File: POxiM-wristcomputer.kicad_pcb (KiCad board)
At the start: 4 copper layers, 40 x 23.5 mm, 62 parts, among them J1 USB_B_Micro, J2 AudioJack4_Ground, U1 LM321, U2 STM8S003F3P

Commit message: Finish display tester board Rev A
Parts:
- removed C1, C3, C5, C8, C9: 100nF, Capacitor_SMD:C_0603_1608Metric
- removed C2: 100pF, Capacitor_SMD:C_0603_1608Metric
- removed C4, C6: 2.2uF, Capacitor_SMD:C_0805_2012Metric
- removed C7: 470nF, Capacitor_SMD:C_0603_1608Metric
- removed D1, D3, D31, D5: 5.2V, Diode_SMD:D_SOD-123
- removed D2, D32, D4, D6: ~, Diode_SMD:D_SOD-323
- removed F1: 100mA, Resistor_SMD:R_1206_3216Metric
- removed FB1: Ferrite_Bead_Small, Inductor_SMD:L_0805_2012Metric
- removed JP1, JP2: Jumper_2_Open, Resistor_SMD:R_0603_1608Metric
- removed R1: 3.3MΩ, Resistor_SMD:R_0805_2012Metric
- removed R2: 1k, Resistor_SMD:R_0805_2012Metric
- removed R3, R4, R5: 100, Resistor_SMD:R_0805_2012Metric
- removed R6: R_Small, Resistor_SMD:R_0805_2012Metric
- removed U1: LM321, Package_TO_SOT_SMD:SOT-23-5
- removed U2: STM8S003F3P, Package_SO:TSSOP-20_4.4x6.5mm_P0.65mm
- added G***: LOGO, POxiM-logos:TUDelftLogo_W10mm, F.Cu at (86.4, 142.8)
- added G***: LOGO, POxiM-logos:POxiMLogo_GoldHeart_W7_5mm, F.Cu at (78.7, 123.0)
- added J14: Jumper_NO_Small, POxiM-uncategorised:SolderJumper-2_P1.3mm_Open_RoundedPad1.0x1.5mm, B.Cu at (99.7, 143.6)
- added JP10: Jumper_NC_Small, POxiM-uncategorised:SolderJumper-2_P1.3mm_SolderBridged_RoundedPad1.0x1.5mm, B.Cu at (101.5, 124.0)
- added JP11: Jumper_NC_Small, POxiM-uncategorised:SolderJumper-2_P1.3mm_SolderBridged_RoundedPad1.0x1.5mm, B.Cu at (80.5, 130.2)
- added JP12: Jumper_NC_Small, POxiM-uncategorised:SolderJumper-2_P1.3mm_SolderBridged_RoundedPad1.0x1.5mm, B.Cu at (101.2, 140.8)
- added JP13: Jumper_NC_Small, POxiM-uncategorised:SolderJumper-2_P1.3mm_SolderBridged_RoundedPad1.0x1.5mm, B.Cu at (80.2, 138.5)
- added JP15: Jumper_NC_Small, POxiM-uncategorised:SolderJumper-2_P1.3mm_SolderBridged_RoundedPad1.0x1.5mm, B.Cu at (78.2, 138.5)
- added JP16: Jumper_NO_Small, POxiM-uncategorised:SolderJumper-2_P1.3mm_Open_RoundedPad1.0x1.5mm, B.Cu at (99.2, 140.8)
- added JP17: Jumper_NC_Small, POxiM-uncategorised:SolderJumper-2_P1.3mm_SolderBridged_RoundedPad1.0x1.5mm, B.Cu at (76.2, 138.5)
- added JP18: Jumper_NO_Small, POxiM-uncategorised:SolderJumper-2_P1.3mm_Open_RoundedPad1.0x1.5mm, B.Cu at (95.5, 124.0)
- added JP19: Jumper_NC_Small, POxiM-uncategorised:SolderJumper-2_P1.3mm_SolderBridged_RoundedPad1.0x1.5mm, B.Cu at (78.5, 130.2)
- added JP20: Jumper_NO_Small, POxiM-uncategorised:SolderJumper-2_P1.3mm_Open_RoundedPad1.0x1.5mm, B.Cu at (97.5, 124.0)
- added JP21: Jumper_NC_Small, POxiM-uncategorised:SolderJumper-2_P1.3mm_SolderBridged_RoundedPad1.0x1.5mm, B.Cu at (78.2, 135.5)
- added JP22: Jumper_NC_Small, POxiM-uncategorised:SolderJumper-2_P1.3mm_SolderBridged_RoundedPad1.0x1.5mm, B.Cu at (90.0, 123.0)
- added JP23: Jumper_NC_Small, POxiM-uncategorised:SolderJumper-2_P1.3mm_SolderBridged_RoundedPad1.0x1.5mm, B.Cu at (75.8, 127.0)
- added JP24: Jumper_NC_Small, POxiM-uncategorised:SolderJumper-2_P1.3mm_SolderBridged_RoundedPad1.0x1.5mm, B.Cu at (93.5, 124.0)
- added JP25: Jumper_NC_Small, POxiM-uncategorised:SolderJumper-2_P1.3mm_SolderBridged_RoundedPad1.0x1.5mm, B.Cu at (103.5, 124.0)
- added JP26: Jumper_NC_Small, POxiM-uncategorised:SolderJumper-2_P1.3mm_SolderBridged_RoundedPad1.0x1.5mm, B.Cu at (89.8, 137.2)
- added JP27: Jumper_NO_Small, POxiM-uncategorised:SolderJumper-2_P1.3mm_Open_RoundedPad1.0x1.5mm, B.Cu at (103.2, 140.8)
- added JP28: Jumper_NO_Small, POxiM-uncategorised:SolderJumper-2_P1.3mm_Open_RoundedPad1.0x1.5mm, B.Cu at (90.0, 143.5)
- added JP29: Jumper_NO_Small, POxiM-uncategorised:SolderJumper-2_P1.3mm_Open_RoundedPad1.0x1.5mm, B.Cu at (87.2, 137.2)
- added JP30: Jumper_NO_Small, POxiM-uncategorised:SolderJumper-2_P1.3mm_Open_RoundedPad1.0x1.5mm, B.Cu at (88.8, 129.2)
- added JP31: Jumper_NO_Small, POxiM-uncategorised:SolderJumper-2_P1.3mm_Open_RoundedPad1.0x1.5mm, B.Cu at (91.0, 129.2)
- added JP8: Jumper_NO_Small, POxiM-uncategorised:SolderJumper-2_P1.3mm_Open_RoundedPad1.0x1.5mm, B.Cu at (99.5, 124.0)
- added JP9: Jumper_NC_Small, POxiM-uncategorised:SolderJumper-2_P1.3mm_SolderBridged_RoundedPad1.0x1.5mm, B.Cu at (78.2, 123.0)
- added R10: 4.7kΩ, Resistor_SMD:R_0805_2012Metric_Pad1.15x1.40mm_HandSolder, B.Cu at (82.5, 130.2)
- added R11: 4.7kΩ, Resistor_SMD:R_0805_2012Metric_Pad1.15x1.40mm_HandSolder, B.Cu at (101.2, 137.2)
- added R12: 4.7kΩ, Resistor_SMD:R_0805_2012Metric_Pad1.15x1.40mm_HandSolder, B.Cu at (82.2, 138.5)
- added R13: 4.7kΩ, Resistor_SMD:R_0805_2012Metric_Pad1.15x1.40mm_HandSolder, B.Cu at (103.2, 143.5)
- added R14: 4.7kΩ, Resistor_SMD:R_0805_2012Metric_Pad1.15x1.40mm_HandSolder, B.Cu at (78.2, 141.2)
- added R15: 4.7kΩ, Resistor_SMD:R_0805_2012Metric_Pad1.15x1.40mm_HandSolder, B.Cu at (99.2, 137.2)
- added R16: 4.7kΩ, Resistor_SMD:R_0805_2012Metric_Pad1.15x1.40mm_HandSolder, B.Cu at (74.0, 138.5)
- added R17: 4.7kΩ, Resistor_SMD:R_0805_2012Metric_Pad1.15x1.40mm_HandSolder, B.Cu at (95.5, 127.8)
- added R18: 4.7kΩ, Resistor_SMD:R_0805_2012Metric_Pad1.15x1.40mm_HandSolder, B.Cu at (76.2, 130.2)
- added R19: 4.7kΩ, Resistor_SMD:R_0805_2012Metric_Pad1.15x1.40mm_HandSolder, B.Cu at (97.5, 127.8)
- added R20: 4.7kΩ, Resistor_SMD:R_0805_2012Metric_Pad1.15x1.40mm_HandSolder, B.Cu at (78.2, 133.2)
- added R21: 4.7kΩ, Resistor_SMD:R_0805_2012Metric_Pad1.15x1.40mm_HandSolder, B.Cu at (90.0, 125.2)
- added R22: 4.7kΩ, Resistor_SMD:R_0805_2012Metric_Pad1.15x1.40mm_HandSolder, B.Cu at (72.2, 127.0)
- added R23: 4.7kΩ, Resistor_SMD:R_0805_2012Metric_Pad1.15x1.40mm_HandSolder, B.Cu at (93.5, 127.8)
- added R24: 4.7kΩ, Resistor_SMD:R_0805_2012Metric_Pad1.15x1.40mm_HandSolder, B.Cu at (104.8, 126.8)
- added R25: 4.7kΩ, Resistor_SMD:R_0805_2012Metric_Pad1.15x1.40mm_HandSolder, B.Cu at (92.0, 137.2)
- added R26: 4.7kΩ, Resistor_SMD:R_0805_2012Metric_Pad1.15x1.40mm_HandSolder, B.Cu at (103.2, 137.2)
- added R27: 4.7kΩ, Resistor_SMD:R_0805_2012Metric_Pad1.15x1.40mm_HandSolder, B.Cu at (90.0, 141.2)
- added R28: 4.7kΩ, Resistor_SMD:R_0805_2012Metric_Pad1.15x1.40mm_HandSolder, B.Cu at (85.0, 137.2)
- added R29: 4.7kΩ, Resistor_SMD:R_0805_2012Metric_Pad1.15x1.40mm_HandSolder, B.Cu at (86.5, 129.2)
- added R30: 4.7kΩ, Resistor_SMD:R_0805_2012Metric_Pad1.15x1.40mm_HandSolder, B.Cu at (90.0, 133.2)
- added R8: 4.7kΩ, Resistor_SMD:R_0805_2012Metric_Pad1.15x1.40mm_HandSolder, B.Cu at (78.2, 125.0)
- added R9: 4.7kΩ, Resistor_SMD:R_0805_2012Metric_Pad1.15x1.40mm_HandSolder, B.Cu at (101.5, 127.8)
- R7: value R_Small -> 4.7kΩ; footprint Resistor_SMD:R_0805_2012Metric -> Resistor_SMD:R_0805_2012Metric_Pad1.15x1.40mm_HandSolder
- moved R7 12.2 mm to (99.5, 127.8), turned to 270 degrees
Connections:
- D10 pad 1: /Display/Segment1 -> GND
- D11 pad 1: /Display/Segment2 -> GND
- D12 pad 1: /Display/Segment2 -> GND
- D12 pad 2: Net-(D10-Pad2) -> Net-(D12-Pad2)
- D13 pad 1: /Display/Segment3 -> GND
- D13 pad 2: Net-(D11-Pad2) -> Net-(D13-Pad2)
- D14 pad 1: /Display/Segment3 -> GND
- D14 pad 2: Net-(D10-Pad2) -> Net-(D14-Pad2)
- D15 pad 1: /Display/Segment4 -> GND
- D15 pad 2: Net-(D11-Pad2) -> Net-(D15-Pad2)
- D16 pad 1: /Display/Segment4 -> GND
- D16 pad 2: Net-(D10-Pad2) -> Net-(D16-Pad2)
- D17 pad 1: /Display/Segment5 -> GND
- D17 pad 2: Net-(D11-Pad2) -> Net-(D17-Pad2)
- D18 pad 1: /Display/Segment5 -> GND
- D18 pad 2: Net-(D10-Pad2) -> Net-(D18-Pad2)
- D19 pad 1: /Display/Segment6 -> GND
- D19 pad 2: Net-(D11-Pad2) -> Net-(D19-Pad2)
- D20 pad 1: /Display/Segment6 -> GND
- D20 pad 2: Net-(D10-Pad2) -> Net-(D20-Pad2)
- D21 pad 1: Net-(D11-Pad2) -> GND
- D21 pad 2: /Display/Segment0 -> Net-(D21-Pad2)
- D22 pad 1: Net-(D10-Pad2) -> GND
- D22 pad 2: /Display/Segment0 -> Net-(D22-Pad2)
- D23 pad 1: Net-(D11-Pad2) -> GND
- D23 pad 2: /Display/Segment1 -> Net-(D23-Pad2)
- D24 pad 1: Net-(D10-Pad2) -> GND
- D24 pad 2: /Display/Segment1 -> Net-(D24-Pad2)
- D25 pad 1: Net-(D11-Pad2) -> GND
- D25 pad 2: /Display/Segment2 -> Net-(D25-Pad2)
- D26 pad 1: Net-(D10-Pad2) -> GND
- D26 pad 2: /Display/Segment2 -> Net-(D26-Pad2)
- D27 pad 1: Net-(D11-Pad2) -> GND
- D27 pad 2: /Display/Segment3 -> Net-(D27-Pad2)
- D28 pad 1: Net-(D11-Pad2) -> GND
- D28 pad 2: /Display/Segment4 -> Net-(D28-Pad2)
- D29 pad 1: Net-(D11-Pad2) -> GND
- D29 pad 2: /Display/Segment5 -> Net-(D29-Pad2)
- D30 pad 1: Net-(D11-Pad2) -> GND
- D30 pad 2: /Display/Segment6 -> Net-(D30-Pad2)
- D7 pad 1: /Display/Segment0 -> GND
- D7 pad 2: Net-(D11-Pad2) -> Net-(D7-Pad2)
- D8 pad 1: /Display/Segment0 -> GND
- D8 pad 2: Net-(D10-Pad2) -> Net-(D8-Pad2)
- D9 pad 1: /Display/Segment1 -> GND
- D9 pad 2: Net-(D11-Pad2) -> Net-(D9-Pad2)
- J1 pad 1: /5V_power_input -> +5V
- J1 pad 2: /USB interface/Data- -> Net-(J1-Pad2)
- J1 pad 3: /USB interface/Data+ -> Net-(J1-Pad3)
- J2 pad R1: /Signal conditioning/LEDOut.IR -> Net-(J2-PadR1)
- J2 pad S: /Signal conditioning/PhotoDiode -> Net-(J2-PadS)
- J2 pad T: /Signal conditioning/LEDOut.Red -> Net-(J2-PadT)
- R7 pad 1: /Display/Common1 -> Net-(JP8-Pad2)
- R7 pad 2: Net-(D10-Pad2) -> Net-(D7-Pad2)
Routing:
- net +5V: track 0.00 -> 108.7 mm
- net GND: track 0.00 -> 10.4 mm, vias 0 -> 5
- net Net-(D9-Pad2): track 0.00 -> 8.21 mm, vias 0 -> 1
- net Net-(D23-Pad2): track 0.00 -> 8.07 mm, vias 0 -> 1
- net Net-(D11-Pad2): track 0.00 -> 7.72 mm, vias 0 -> 1
- net Net-(D17-Pad2): track 0.00 -> 7.47 mm, vias 0 -> 1
- net Net-(D7-Pad2): track 0.00 -> 7.12 mm, vias 0 -> 1
- net Net-(D19-Pad2): track 0.00 -> 6.59 mm, vias 0 -> 1
- net Net-(D18-Pad2): track 0.00 -> 6.50 mm, vias 0 -> 1
- net Net-(D26-Pad2): track 0.00 -> 6.11 mm, vias 0 -> 1
- net Net-(D13-Pad2): track 0.00 -> 5.32 mm, vias 0 -> 1
- net Net-(D16-Pad2): track 0.00 -> 5.09 mm, vias 0 -> 1
- net Net-(D25-Pad2): track 0.00 -> 5.07 mm, vias 0 -> 1
- net Net-(D24-Pad2): track 0.00 -> 5.07 mm, vias 0 -> 1
- net Net-(JP30-Pad2): track 0.00 -> 4.78 mm
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- added copper zone on B.Cu, net GND
- added copper zone on F.Cu, net GND
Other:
- net class Default: clearance 0.2 -> 0.1; trace_width 0.25 -> 0.1; via_dia 0.8 -> 0.4; via_drill 0.4 -> 0.2
- rule trace_clearance: 0.2 -> 0.1
- rule trace_min: 0.2 -> 0.1
- rule via_min_drill: 0.3 -> 0.2
- board text added: "Display test board Rev A"

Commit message: Finish works-as prototype design
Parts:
- removed the G*** at (86.4, 142.8)
- removed the G*** at (78.7, 123.0)
- removed J14, JP16, JP18, JP20, JP27, JP28, JP29, JP30, JP31, JP8: Jumper_NO_Small, POxiM-uncategorised:SolderJumper-2_P1.3mm_Open_RoundedPad1.0x1.5mm
- removed JP10, JP11, JP12, JP13, JP15, JP17, JP19, JP21, JP22, JP23, JP24, JP25, JP26, JP9: Jumper_NC_Small, POxiM-uncategorised:SolderJumper-2_P1.3mm_SolderBridged_RoundedPad1.0x1.5mm
- removed R20, R21, R22, R23, R24, R25, R26, R27, R28, R29, R30: 4.7kΩ, Resistor_SMD:R_0805_2012Metric_Pad1.15x1.40mm_HandSolder
- added C1: 100nF, Capacitor_SMD:C_0603_1608Metric, F.Cu at (182.7, 114.8)
- added C10: 2.2uF, Capacitor_SMD:C_0805_2012Metric, B.Cu at (128.0, 65.2)
- added C11: 100nF, Capacitor_SMD:C_0603_1608Metric, B.Cu at (128.0, 63.5)
- added C12: 100nF, Capacitor_SMD:C_0603_1608Metric, B.Cu at (123.2, 48.2)
- added C13: 2.2uF, Capacitor_SMD:C_0805_2012Metric, B.Cu at (121.5, 48.2)
- added C14: 6.8uF, Capacitor_SMD:C_1206_3216Metric, B.Cu at (115.5, 60.5)
- added C15: 6.8uF, Capacitor_SMD:C_1206_3216Metric, B.Cu at (140.5, 60.5)
- added C16: 100nF, Capacitor_SMD:C_0603_1608Metric, B.Cu at (109.2, 60.5)
- added C17: 100nF, Capacitor_SMD:C_0603_1608Metric, B.Cu at (146.8, 60.5)
- added C2: 100pF, Capacitor_SMD:C_0603_1608Metric, F.Cu at (188.2, 114.8)
- added C3: 100nF, Capacitor_SMD:C_0603_1608Metric, F.Cu at (188.2, 119.0)
- added C4: 2.2uF, Capacitor_SMD:C_0805_2012Metric, F.Cu at (182.0, 119.8)
- added C5: 100nF, Capacitor_SMD:C_0603_1608Metric, F.Cu at (171.2, 105.2)
- added C6: 2.2uF, Capacitor_SMD:C_0805_2012Metric, F.Cu at (164.0, 105.2)
- added C7: 470nF, Capacitor_SMD:C_0603_1608Metric, F.Cu at (168.8, 105.2)
- added C8: 100nF, Capacitor_SMD:C_0603_1608Metric, F.Cu at (165.8, 105.2)
- added C9: 100nF, Capacitor_SMD:C_0603_1608Metric, F.Cu at (167.2, 105.2)
- added D1: 5.2V, Diode_SMD:D_SOD-123, F.Cu at (176.5, 138.2)
- added D2: ~, Diode_SMD:D_SOD-323, F.Cu at (175.8, 136.0)
- added D3: 5.2V, Diode_SMD:D_SOD-123, F.Cu at (176.5, 127.0)
- added D31: 5.2V, Diode_SMD:D_SOD-123, F.Cu at (156.2, 134.5)
- added D32: ~, Diode_SMD:D_SOD-323, F.Cu at (155.8, 132.2)
- added D4: ~, Diode_SMD:D_SOD-323, F.Cu at (175.8, 129.2)
- added D5: 5.2V, Diode_SMD:D_SOD-123, F.Cu at (181.2, 122.0)
- added D6: ~, Diode_SMD:D_SOD-323, F.Cu at (177.2, 124.5)
- added F1: 100mA, Resistor_SMD:R_1206_3216Metric, F.Cu at (156.2, 137.0)
- added FB1: Ferrite_Bead_Small, Inductor_SMD:L_0603_1608Metric, F.Cu at (161.5, 106.0)
- added G***: LOGO, POxiM-logos:POxiMLogo_GoldHeart_W10mm, F.Cu at (120.0, 129.8)
- added G***: LOGO, POxiM-logos:TUDelftLogo_W10mm, F.Cu at (119.2, 132.8)
- added G***: LOGO, POxiM-logos:TUDelftLogo_W10mm, F.Cu at (157.8, 125.8)
- added G***: LOGO, POxiM-logos:POxiMLogo_GoldHeart_W10mm, F.Cu at (154.8, 125.0)
- added G***: LOGO, POxiM-logos:TUDelftLogo_W10mm, F.Cu at (184.2, 44.2)
- added G***: LOGO, POxiM-logos:POxiMLogo_GoldHeart_W20mm, F.Cu at (119.2, 44.0)
- added J10: Transmissivity in, Connector_Coaxial:SMA_Molex_73251-2200_Horizontal, F.Cu at (95.0, 60.5)
- added J11: AudioJack4_Ground, POxiM-uncategorised:CUI_SJ-43514-SMT, F.Cu at (98.5, 45.5)
- added J3: USB_B_Micro, POxiM-uncategorised:Micro-B_Molex_105017-0001, F.Cu at (115.0, 140.0)
- added J4: USB_A, POxiM-uncategorised:USBA_87583-2010RLF, F.Cu at (104.0, 131.0)
- added J5: USB_A, POxiM-uncategorised:USBA_87583-2010RLF, F.Cu at (104.0, 109.0)
- added J6: Uart Out, Connector_PinHeader_2.54mm:PinHeader_1x02_P2.54mm_Vertical, F.Cu at (108.0, 118.7)
- added J7: Programming Header, Connector_PinHeader_2.54mm:PinHeader_2x05_P2.54mm_Vertical, F.Cu at (123.2, 118.7)
- added J8: USB_B_Micro, POxiM-uncategorised:Micro-B_Molex_105017-0001, F.Cu at (90.0, 91.0)
- added J9: Interference in, Connector_Coaxial:SMA_Molex_73251-2200_Horizontal, F.Cu at (95.0, 76.0)
- added JP1: Jumper_2_Open, Resistor_SMD:R_0603_1608Metric, F.Cu at (164.8, 132.8)
- added JP2: Jumper_2_Open, Resistor_SMD:R_0603_1608Metric, F.Cu at (163.0, 132.8)
- added MB1: Bumpon, POxiM-uncategorised:Bumpon-SJ-5007BK, B.Cu at (96.0, 131.0)
- added MB10: Bumpon, POxiM-uncategorised:Bumpon-SJ-5007BK, B.Cu at (184.0, 46.0)
- added MB11: Bumpon, POxiM-uncategorised:Bumpon-SJ-5007BK, B.Cu at (184.0, 91.5)
- added MB12: Bumpon, POxiM-uncategorised:Bumpon-SJ-5007BK, B.Cu at (96.0, 91.5)
- added MB2: Bumpon, POxiM-uncategorised:Bumpon-SJ-5007BK, B.Cu at (96.0, 109.0)
- added MB3: Bumpon, POxiM-uncategorised:Bumpon-SJ-5007BK, B.Cu at (121.0, 106.0)
- added MB4: Bumpon, POxiM-uncategorised:Bumpon-SJ-5007BK, B.Cu at (121.0, 134.0)
- added MB5: Bumpon, POxiM-uncategorised:Bumpon-SJ-5007BK, B.Cu at (139.5, 134.2)
- added MB6: Bumpon, POxiM-uncategorised:Bumpon-SJ-5007BK, B.Cu at (139.5, 105.8)
- added MB7: Bumpon, POxiM-uncategorised:Bumpon-SJ-5007BK, B.Cu at (184.0, 134.0)
- added MB8: Bumpon, POxiM-uncategorised:Bumpon-SJ-5007BK, B.Cu at (184.0, 106.0)
- added MB9: Bumpon, POxiM-uncategorised:Bumpon-SJ-5007BK, B.Cu at (96.0, 46.0)
- added R1: 3.3MΩ, Resistor_SMD:R_0805_2012Metric, F.Cu at (185.5, 117.8)
- added R2: 1k, Resistor_SMD:R_0805_2012Metric, F.Cu at (185.5, 119.8)
- added R3: 100, Resistor_SMD:R_0805_2012Metric, F.Cu at (185.5, 122.0)
- added R4: 100, Resistor_SMD:R_0805_2012Metric, F.Cu at (175.8, 131.2)
- added R5: 100, Resistor_SMD:R_0805_2012Metric, F.Cu at (175.8, 134.0)
- added R6: R_Small, Resistor_SMD:R_0805_2012Metric, F.Cu at (162.0, 111.5)
- added RV1: 1k, POxiM-uncategorised:Potentiometer_Bourns_PTV09A-1_Single_Vertical, F.Cu at (170.5, 64.0)
- added RV2: 1k, POxiM-uncategorised:Potentiometer_Bourns_PTV09A-1_Single_Vertical, F.Cu at (118.0, 64.0)
- added RV3: 1k, POxiM-uncategorised:Potentiometer_Bourns_PTV09A-1_Single_Vertical, F.Cu at (118.0, 91.0)
- added RV4: 1k, POxiM-uncategorised:Potentiometer_Bourns_PTV09A-1_Single_Vertical, F.Cu at (143.0, 64.0)
- added RV5: 1k, POxiM-uncategorised:Potentiometer_Bourns_PTV09A-1_Single_Vertical, F.Cu at (143.0, 91.0)
- added SW1: Current range, POxiM-uncategorised:SW_ESwitch_KC14A10.001NPS, F.Cu at (168.0, 81.5)
- added TP1: LED_IR, TestPoint:TestPoint_Loop_D2.60mm_Drill1.4mm_Beaded, F.Cu at (166.0, 119.0)
- added TP10: IR, TestPoint:TestPoint_Loop_D2.60mm_Drill1.4mm_Beaded, F.Cu at (147.5, 46.2)
- added TP11: R, TestPoint:TestPoint_Loop_D2.60mm_Drill1.4mm_Beaded, F.Cu at (171.5, 46.2)
- added TP12: IR, TestPoint:TestPoint_Loop_D2.60mm_Drill1.4mm_Beaded, F.Cu at (175.5, 46.2)
- added TP13: I_in, TestPoint:TestPoint_Loop_D2.60mm_Drill1.4mm_Beaded, F.Cu at (159.5, 46.2)
- added TP16: N, TestPoint:TestPoint_Loop_D2.60mm_Drill1.4mm_Beaded, F.Cu at (167.5, 46.2)
- added TP17: R, TestPoint:TestPoint_Loop_D2.60mm_Drill1.4mm_Beaded, F.Cu at (139.5, 46.2)
- added TP19: GND, TestPoint:TestPoint_Loop_D2.60mm_Drill1.4mm_Beaded, F.Cu at (162.0, 119.0)
- added TP2: LED_R, TestPoint:TestPoint_Loop_D2.60mm_Drill1.4mm_Beaded, F.Cu at (170.0, 119.0)
- added TP20: GND, TestPoint:TestPoint_Loop_D2.60mm_Drill1.4mm_Beaded, F.Cu at (182.5, 110.5)
- added TP3: ADC_FB, TestPoint:TestPoint_Loop_D2.60mm_Drill1.4mm_Beaded, F.Cu at (178.5, 117.8)
- added TP4: ADC_in, TestPoint:TestPoint_Loop_D2.60mm_Drill1.4mm_Beaded, F.Cu at (186.5, 110.5)
- added TP5: PD3, TestPoint:TestPoint_Loop_D2.60mm_Drill1.4mm_Beaded, F.Cu at (176.8, 109.8)
- added TP6: PD4, TestPoint:TestPoint_Loop_D2.60mm_Drill1.4mm_Beaded, F.Cu at (176.8, 105.8)
- added TP7: PD2, TestPoint:TestPoint_Loop_D2.60mm_Drill1.4mm_Beaded, F.Cu at (176.8, 113.8)
- added TP8: GND, TestPoint:TestPoint_Loop_D2.60mm_Drill1.4mm_Beaded, F.Cu at (143.5, 46.2)
- added TP9: GND, TestPoint:TestPoint_Loop_D2.60mm_Drill1.4mm_Beaded, F.Cu at (163.5, 46.2)
- added U1: LM321, Package_TO_SOT_SMD:SOT-23-5, F.Cu at (185.5, 114.8)
- added U2: STM8S003F3P, Package_SO:TSSOP-20_4.4x6.5mm_P0.65mm, F.Cu at (170.2, 110.8)
- added U3: LM358, Package_SO:SOIC-8_3.9x4.9mm_P1.27mm, B.Cu at (128.0, 60.0)
- added U4: NLAS4053, Package_SO:SOIC-16_3.9x9.9mm_P1.27mm, B.Cu at (128.0, 51.8)
- added mouse-bite-2.54mm-slot: VAL**, Panelization:mouse-bite-2.5mm-slot, F.Cu at (96.5, 98.8)
- added mouse-bite-2.54mm-slot: VAL**, Panelization:mouse-bite-2.5mm-slot, F.Cu at (128.2, 133.5)
- added mouse-bite-2.54mm-slot: VAL**, Panelization:mouse-bite-2.5mm-slot, F.Cu at (128.2, 106.5)
- added mouse-bite-2.54mm-slot: VAL**, Panelization:mouse-bite-2.5mm-slot, F.Cu at (120.5, 98.8)
- added mouse-bite-2.54mm-slot: VAL**, Panelization:mouse-bite-2.5mm-slot, F.Cu at (136.0, 98.8)
- added mouse-bite-2.54mm-slot: VAL**, Panelization:mouse-bite-2.5mm-slot, F.Cu at (183.5, 98.8)
- J1, J2: moved to F.Cu
- R10, R18, R19, R8, R9: value 4.7kΩ -> 27kΩ; footprint Resistor_SMD:R_0805_2012Metric_Pad1.15x1.40mm_HandSolder -> Resistor_SMD:R_0603_1608Metric
- R11: value 4.7kΩ -> 1kΩ; footprint Resistor_SMD:R_0805_2012Metric_Pad1.15x1.40mm_HandSolder -> Resistor_SMD:R_0603_1608Metric
- R12: value 4.7kΩ -> 4.7MΩ; footprint Resistor_SMD:R_0805_2012Metric_Pad1.15x1.40mm_HandSolder -> Resistor_SMD:R_0603_1608Metric
- R13: value 4.7kΩ -> 470kΩ; footprint Resistor_SMD:R_0805_2012Metric_Pad1.15x1.40mm_HandSolder -> Resistor_SMD:R_0603_1608Metric
- R14: value 4.7kΩ -> 47kΩ; footprint Resistor_SMD:R_0805_2012Metric_Pad1.15x1.40mm_HandSolder -> Resistor_SMD:R_0603_1608Metric
- R15: footprint Resistor_SMD:R_0805_2012Metric_Pad1.15x1.40mm_HandSolder -> Resistor_SMD:R_0603_1608Metric
- R16, R17: value 4.7kΩ -> 510k; footprint Resistor_SMD:R_0805_2012Metric_Pad1.15x1.40mm_HandSolder -> Resistor_SMD:R_0603_1608Metric
- R7: value 4.7kΩ -> R_Small; footprint Resistor_SMD:R_0805_2012Metric_Pad1.15x1.40mm_HandSolder -> Resistor_SMD:R_0805_2012Metric; moved to F.Cu
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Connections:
- D10 pad 1: GND -> /Display/Segment1
- D11 pad 1: GND -> /Display/Segment2
- D12 pad 1: GND -> /Display/Segment2
- D12 pad 2: Net-(D12-Pad2) -> Net-(D10-Pad2)
- D13 pad 1: GND -> /Display/Segment3
- D13 pad 2: Net-(D13-Pad2) -> Net-(D11-Pad2)
- D14 pad 1: GND -> /Display/Segment3
- D14 pad 2: Net-(D14-Pad2) -> Net-(D10-Pad2)
- D15 pad 1: GND -> /Display/Segment4
- D15 pad 2: Net-(D15-Pad2) -> Net-(D11-Pad2)
- D16 pad 1: GND -> /Display/Segment4
- D16 pad 2: Net-(D16-Pad2) -> Net-(D10-Pad2)
- D17 pad 1: GND -> /Display/Segment5
- D17 pad 2: Net-(D17-Pad2) -> Net-(D11-Pad2)
- D18 pad 1: GND -> /Display/Segment5
- D18 pad 2: Net-(D18-Pad2) -> Net-(D10-Pad2)
- D19 pad 1: GND -> /Display/Segment6
- D19 pad 2: Net-(D19-Pad2) -> Net-(D11-Pad2)
- D20 pad 1: GND -> /Display/Segment6
- D20 pad 2: Net-(D20-Pad2) -> Net-(D10-Pad2)
- D21 pad 1: GND -> Net-(D11-Pad2)
- D21 pad 2: Net-(D21-Pad2) -> /Display/Segment0
- D22 pad 1: GND -> Net-(D10-Pad2)
- D22 pad 2: Net-(D22-Pad2) -> /Display/Segment0
- D23 pad 1: GND -> Net-(D11-Pad2)
- D23 pad 2: Net-(D23-Pad2) -> /Display/Segment1
- D24 pad 1: GND -> Net-(D10-Pad2)
- D24 pad 2: Net-(D24-Pad2) -> /Display/Segment1
- D25 pad 1: GND -> Net-(D11-Pad2)
- D25 pad 2: Net-(D25-Pad2) -> /Display/Segment2
- D26 pad 1: GND -> Net-(D10-Pad2)
- D26 pad 2: Net-(D26-Pad2) -> /Display/Segment2
- D27 pad 1: GND -> Net-(D11-Pad2)
- D27 pad 2: Net-(D27-Pad2) -> /Display/Segment3
- D28 pad 1: GND -> Net-(D11-Pad2)
- D28 pad 2: Net-(D28-Pad2) -> /Display/Segment4
- D29 pad 1: GND -> Net-(D11-Pad2)
- D29 pad 2: Net-(D29-Pad2) -> /Display/Segment5
- D30 pad 1: GND -> Net-(D11-Pad2)
- D30 pad 2: Net-(D30-Pad2) -> /Display/Segment6
- D7 pad 1: GND -> /Display/Segment0
- D7 pad 2: Net-(D7-Pad2) -> Net-(D11-Pad2)
- D8 pad 1: GND -> /Display/Segment0
- D8 pad 2: Net-(D8-Pad2) -> Net-(D10-Pad2)
- D9 pad 1: GND -> /Display/Segment1
- D9 pad 2: Net-(D9-Pad2) -> Net-(D11-Pad2)
- J1 pad 1: +5V -> /5V_power_input
- J1 pad 2: Net-(J1-Pad2) -> /USB interface/Data-
- J1 pad 3: Net-(J1-Pad3) -> /USB interface/Data+
- J2 pad R1: Net-(J2-PadR1) -> /Signal conditioning/LEDOut.IR
- J2 pad S: Net-(J2-PadS) -> /Signal conditioning/PhotoDiode
- J2 pad T: Net-(J2-PadT) -> /Signal conditioning/LEDOut.Red
- R10 pad 1: Net-(JP11-Pad2) -> Net-(R10-Pad1)
- R10 pad 2: Net-(D10-Pad2) -> Net-(R10-Pad2)
- R11 pad 1: Net-(JP12-Pad2) -> /Testing finger board/GND
- R11 pad 2: Net-(D11-Pad2) -> Net-(R10-Pad1)
- R12 pad 1: Net-(JP13-Pad2) -> /Testing finger board/Photodiode
- R12 pad 2: Net-(D12-Pad2) -> Net-(R12-Pad2)
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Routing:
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- added copper zone on B.Cu, net /Testing finger board/GND
- added copper zone on F.Cu, net /Testing finger board/GND
- added copper zone on B.Cu, net Net-(J3-Pad5)
- added copper zone on F.Cu, net Net-(J3-Pad5)
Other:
- board size 40 x 23.5 mm -> 100 x 100 mm
- board text added: "0"
- board text added: "0.1µA"
- board text added: "1"
- board text added: "10"
- board text added: "100µA"
- board text added: "10µA"
- board text added: "1µA"
- board text added: "2"
- board text added: "3"
- board text added: "4"
- board text added: "5"
- board text added: "6"
- board text added: "7"
- board text added: "8"
- board text added: "9"
- board text added: "Current range"
- board text added: "Development board Rev A"
- board text added: "Finger simulator Rev A"
- board text added: "GND"
- board text added: "Infrared bias"
- board text added: "Infrared scale"
- board text added: "MIX"
- board text added: "Noise scale"
- board text added: "Programming adapter Rev A"
- board text added: "Red bias"
- board text added: "Red scale"
- board text added: "SWIM"
- board text added: "Simulated transmissivity"
- board text added: "ToDo: - Run DRC - Add potentiometer knobs to BOM"
- board text added: "UART.TX"
- board text removed: "Display test board Rev A"

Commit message: Finalise works-like prototype
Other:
- copper layers 4 -> 2
- board text removed: "ToDo: - Run DRC - Add potentiometer knobs to BOM"

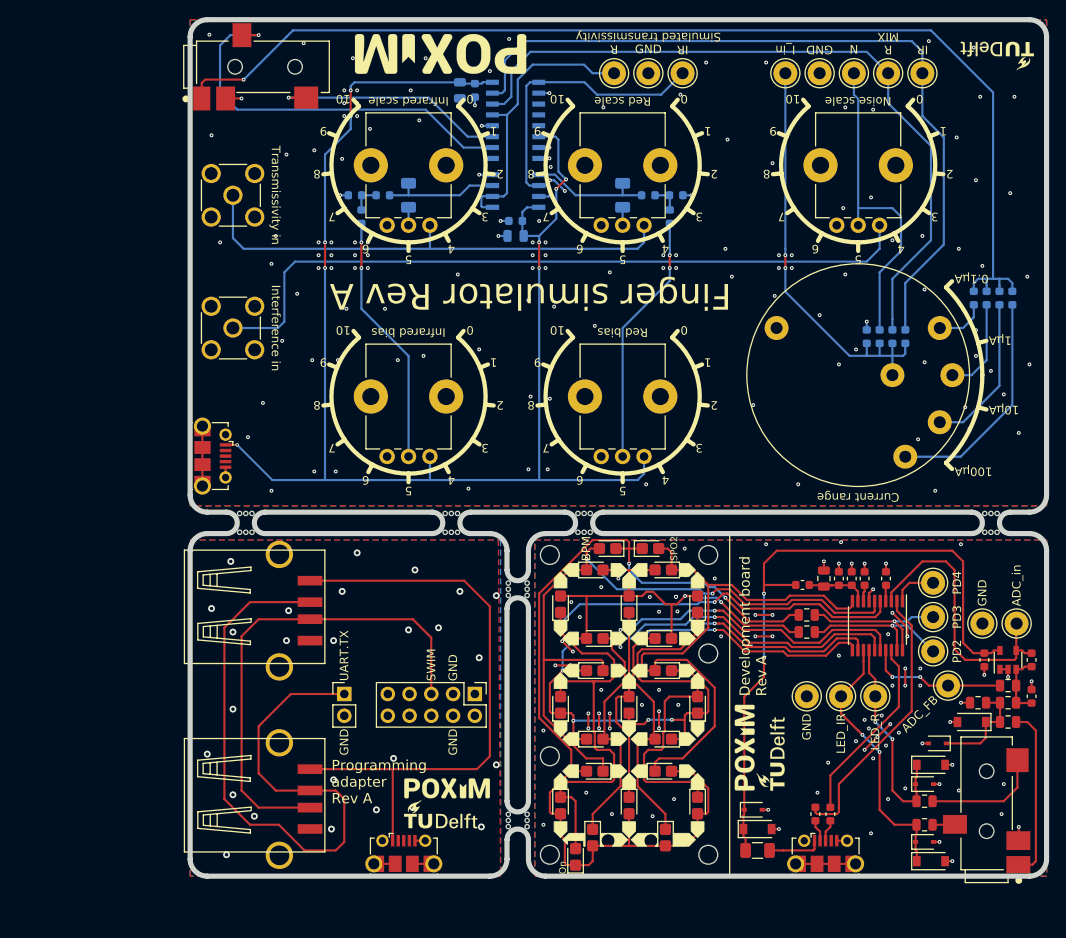
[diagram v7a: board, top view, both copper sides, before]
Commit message: Start new LED drive method, some cleanup
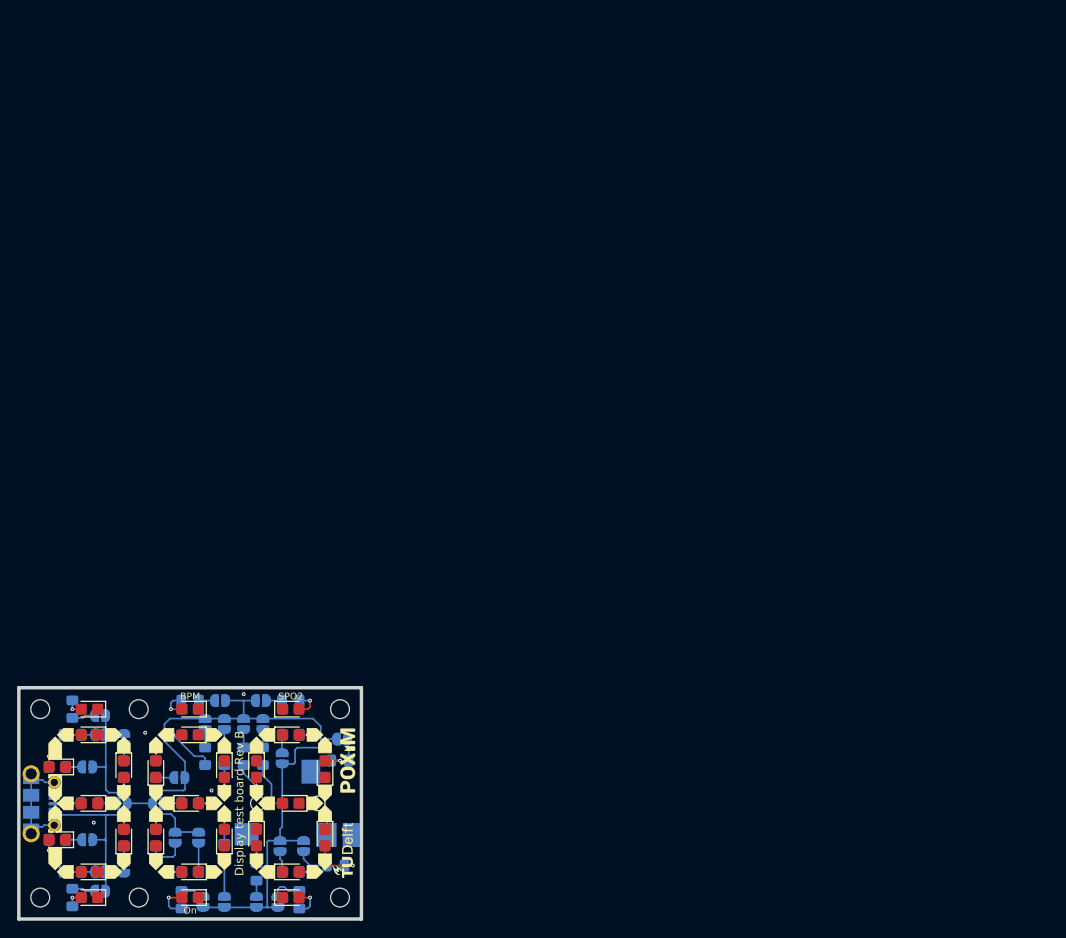
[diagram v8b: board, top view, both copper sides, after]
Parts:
- removed C1, C11, C12, C16, C17, C3, C5, C8, C9: 100nF, Capacitor_SMD:C_0603_1608Metric
- removed C10, C13, C4, C6: 2.2uF, Capacitor_SMD:C_0805_2012Metric
- removed C14, C15: 6.8uF, Capacitor_SMD:C_1206_3216Metric
- removed C2: 100pF, Capacitor_SMD:C_0603_1608Metric
- removed C7: 470nF, Capacitor_SMD:C_0603_1608Metric
- removed D31, D5: 5.2V, Diode_SMD:D_SOD-123
- removed D32, D4, D6: ~, Diode_SMD:D_SOD-323
- removed F1: 100mA, Resistor_SMD:R_1206_3216Metric
- removed FB1: Ferrite_Bead_Small, Inductor_SMD:L_0603_1608Metric
- removed the G*** at (120.0, 129.8)
- removed the G*** at (119.2, 132.8)
- removed the G*** at (157.8, 125.8)
- removed the G*** at (154.8, 125.0)
- removed the G*** at (184.2, 44.2)
- removed the G*** at (119.2, 44.0)
- removed J10: Transmissivity in, Connector_Coaxial:SMA_Molex_73251-2200_Horizontal
- removed J11: AudioJack4_Ground, POxiM-uncategorised:CUI_SJ-43514-SMT
- removed J3, J8: USB_B_Micro, POxiM-uncategorised:Micro-B_Molex_105017-0001
- removed J4, J5: USB_A, POxiM-uncategorised:USBA_87583-2010RLF
- removed J6: Uart Out, Connector_PinHeader_2.54mm:PinHeader_1x02_P2.54mm_Vertical
- removed J7: Programming Header, Connector_PinHeader_2.54mm:PinHeader_2x05_P2.54mm_Vertical
- removed J9: Interference in, Connector_Coaxial:SMA_Molex_73251-2200_Horizontal
- removed MB1, MB10, MB11, MB12, MB2, MB3, MB4, MB5, MB6, MB7, MB8, MB9: Bumpon, POxiM-uncategorised:Bumpon-SJ-5007BK
- removed R4, R5: 100, Resistor_SMD:R_0805_2012Metric
- removed R6: R_Small, Resistor_SMD:R_0805_2012Metric
- removed RV1, RV2, RV3, RV4, RV5: 1k, POxiM-uncategorised:Potentiometer_Bourns_PTV09A-1_Single_Vertical
- removed SW1: Current range, POxiM-uncategorised:SW_ESwitch_KC14A10.001NPS
- removed TP1: LED_IR, TestPoint:TestPoint_Loop_D2.60mm_Drill1.4mm_Beaded
- removed TP10, TP12: IR, TestPoint:TestPoint_Loop_D2.60mm_Drill1.4mm_Beaded
- removed TP11, TP17: R, TestPoint:TestPoint_Loop_D2.60mm_Drill1.4mm_Beaded
- removed TP13: I_in, TestPoint:TestPoint_Loop_D2.60mm_Drill1.4mm_Beaded
- removed TP16: N, TestPoint:TestPoint_Loop_D2.60mm_Drill1.4mm_Beaded
- removed TP19, TP20, TP8, TP9: GND, TestPoint:TestPoint_Loop_D2.60mm_Drill1.4mm_Beaded
- removed TP2: LED_R, TestPoint:TestPoint_Loop_D2.60mm_Drill1.4mm_Beaded
- removed TP3: ADC_FB, TestPoint:TestPoint_Loop_D2.60mm_Drill1.4mm_Beaded
- removed TP4: ADC_in, TestPoint:TestPoint_Loop_D2.60mm_Drill1.4mm_Beaded
- removed TP5: PD3, TestPoint:TestPoint_Loop_D2.60mm_Drill1.4mm_Beaded
- removed TP6: PD4, TestPoint:TestPoint_Loop_D2.60mm_Drill1.4mm_Beaded
- removed TP7: PD2, TestPoint:TestPoint_Loop_D2.60mm_Drill1.4mm_Beaded
- removed U1: LM321, Package_TO_SOT_SMD:SOT-23-5
- removed U2: STM8S003F3P, Package_SO:TSSOP-20_4.4x6.5mm_P0.65mm
- removed U3: LM358, Package_SO:SOIC-8_3.9x4.9mm_P1.27mm
- removed U4: NLAS4053, Package_SO:SOIC-16_3.9x9.9mm_P1.27mm
- removed mouse-bite-2.54mm-slot (x6): VAL**, Panelization:mouse-bite-2.5mm-slot
- added G***: LOGO, POxiM-logos:TUDelftLogo_W7_5mm, F.Cu at (107.8, 137.0)
- added G***: LOGO, POxiM-logos:POxiMLogo_GoldHeart_W7_5mm, F.Cu at (108.4, 126.5)
- added J14: Jumper_NO_Small, POxiM-uncategorised:SolderJumper-2_P1.3mm_Open_RoundedPad1.0x1.5mm, B.Cu at (100.5, 136.5)
- added JP10: Jumper_NC_Small, POxiM-uncategorised:SolderJumper-2_P1.3mm_SolderBridged_RoundedPad1.0x1.5mm, B.Cu at (107.8, 124.0)
- added JP11: Jumper_NC_Small, POxiM-uncategorised:SolderJumper-2_P1.3mm_SolderBridged_RoundedPad1.0x1.5mm, B.Cu at (82.2, 124.0)
- added JP12: Jumper_NC_Small, POxiM-uncategorised:SolderJumper-2_P1.3mm_SolderBridged_RoundedPad1.0x1.5mm, B.Cu at (103.2, 136.5)
- added JP13: Jumper_NC_Small, POxiM-uncategorised:SolderJumper-2_P1.3mm_SolderBridged_RoundedPad1.0x1.5mm, B.Cu at (82.2, 139.0)
- added JP15: Jumper_NC_Small, POxiM-uncategorised:SolderJumper-2_P1.3mm_SolderBridged_RoundedPad1.0x1.5mm, B.Cu at (79.5, 139.5)
- added JP16: Jumper_NO_Small, POxiM-uncategorised:SolderJumper-2_P1.3mm_Open_RoundedPad1.0x1.5mm, B.Cu at (97.8, 143.0)
- added JP17: Jumper_NC_Small, POxiM-uncategorised:SolderJumper-2_P1.3mm_SolderBridged_RoundedPad1.0x1.5mm, B.Cu at (78.0, 135.8)
- added JP18: Jumper_NO_Small, POxiM-uncategorised:SolderJumper-2_P1.3mm_Open_RoundedPad1.0x1.5mm, B.Cu at (96.2, 122.2)
- added JP19: Jumper_NC_Small, POxiM-uncategorised:SolderJumper-2_P1.3mm_SolderBridged_RoundedPad1.0x1.5mm, B.Cu at (78.0, 127.2)
- added JP20: Jumper_NO_Small, POxiM-uncategorised:SolderJumper-2_P1.3mm_Open_RoundedPad1.0x1.5mm, B.Cu at (98.5, 122.2)
- added JP21: Jumper_NC_Small, POxiM-uncategorised:SolderJumper-2_P1.3mm_SolderBridged_RoundedPad1.0x1.5mm, B.Cu at (82.0, 131.5)
- added JP22: Jumper_NC_Small, POxiM-uncategorised:SolderJumper-2_P1.3mm_SolderBridged_RoundedPad1.0x1.5mm, B.Cu at (91.8, 122.2)
- added JP23: Jumper_NC_Small, POxiM-uncategorised:SolderJumper-2_P1.3mm_SolderBridged_RoundedPad1.0x1.5mm, B.Cu at (91.5, 143.0)
- added JP24: Jumper_NC_Small, POxiM-uncategorised:SolderJumper-2_P1.3mm_SolderBridged_RoundedPad1.0x1.5mm, B.Cu at (94.0, 122.2)
- added JP25: Jumper_NC_Small, POxiM-uncategorised:SolderJumper-2_P1.3mm_SolderBridged_RoundedPad1.0x1.5mm, B.Cu at (93.5, 119.5)
- added JP26: Jumper_NC_Small, POxiM-uncategorised:SolderJumper-2_P1.3mm_SolderBridged_RoundedPad1.0x1.5mm, B.Cu at (94.0, 143.0)
- added JP27: Jumper_NO_Small, POxiM-uncategorised:SolderJumper-2_P1.3mm_Open_RoundedPad1.0x1.5mm, B.Cu at (98.2, 119.5)
- added JP28: Jumper_NO_Small, POxiM-uncategorised:SolderJumper-2_P1.3mm_Open_RoundedPad1.0x1.5mm, B.Cu at (91.0, 135.5)
- added JP29: Jumper_NO_Small, POxiM-uncategorised:SolderJumper-2_P1.3mm_Open_RoundedPad1.0x1.5mm, B.Cu at (88.2, 135.5)
- added JP3: Jumper_NO_Small, POxiM-uncategorised:SolderJumper-2_P1.3mm_Open_RoundedPad1.0x1.5mm, B.Cu at (100.2, 143.0)
- added JP30: Jumper_NO_Small, POxiM-uncategorised:SolderJumper-2_P1.3mm_Open_RoundedPad1.0x1.5mm, B.Cu at (88.8, 128.5)
- added JP31: Jumper_NO_Small, POxiM-uncategorised:SolderJumper-2_P1.3mm_Open_RoundedPad1.0x1.5mm, B.Cu at (86.2, 131.5)
- added JP8: Jumper_NO_Small, POxiM-uncategorised:SolderJumper-2_P1.3mm_Open_RoundedPad1.0x1.5mm, B.Cu at (100.8, 126.2)
- added JP9: Jumper_NC_Small, POxiM-uncategorised:SolderJumper-2_P1.3mm_SolderBridged_RoundedPad1.0x1.5mm, B.Cu at (79.5, 123.5)
- added R20: 4.7kΩ, Resistor_SMD:R_0805_2012Metric_Pad1.15x1.40mm_HandSolder, B.Cu at (78.2, 131.5)
- added R21: 4.7kΩ, Resistor_SMD:R_0805_2012Metric_Pad1.15x1.40mm_HandSolder, B.Cu at (91.8, 126.0)
- added R22: 4.7kΩ, Resistor_SMD:R_0805_2012Metric_Pad1.15x1.40mm_HandSolder, B.Cu at (89.0, 142.8)
- added R23: 4.7kΩ, Resistor_SMD:R_0805_2012Metric_Pad1.15x1.40mm_HandSolder, B.Cu at (94.0, 126.0)
- added R24: 4.7kΩ, Resistor_SMD:R_0805_2012Metric_Pad1.15x1.40mm_HandSolder, B.Cu at (90.0, 119.5)
- added R25: 4.7kΩ, Resistor_SMD:R_0805_2012Metric_Pad1.15x1.40mm_HandSolder, B.Cu at (94.0, 137.2)
- added R26: 4.7kΩ, Resistor_SMD:R_0805_2012Metric_Pad1.15x1.40mm_HandSolder, B.Cu at (101.8, 119.5)
- added R27: 4.7kΩ, Resistor_SMD:R_0805_2012Metric_Pad1.15x1.40mm_HandSolder, B.Cu at (90.0, 139.5)
- added R28: 4.7kΩ, Resistor_SMD:R_0805_2012Metric_Pad1.15x1.40mm_HandSolder, B.Cu at (86.0, 135.5)
- added R29: 4.7kΩ, Resistor_SMD:R_0805_2012Metric_Pad1.15x1.40mm_HandSolder, B.Cu at (86.0, 127.5)
- added R30: 4.7kΩ, Resistor_SMD:R_0805_2012Metric_Pad1.15x1.40mm_HandSolder, B.Cu at (90.0, 131.5)
- D1, D3: value 5.2V -> LED; footprint Diode_SMD:D_SOD-123 -> LED_SMD:LED_0805_2012Metric_Castellated
- D2: value ~ -> LED; footprint Diode_SMD:D_SOD-323 -> LED_SMD:LED_0805_2012Metric_Castellated
- J1, J2: moved to B.Cu
- JP1, JP2: value Jumper_2_Open -> Jumper_NO_Small; footprint Resistor_SMD:R_0603_1608Metric -> POxiM-uncategorised:SolderJumper-2_P1.3mm_Open_RoundedPad1.0x1.5mm; moved to B.Cu
- R1: value 3.3MΩ -> 4.7kΩ; footprint Resistor_SMD:R_0805_2012Metric -> Resistor_SMD:R_0805_2012Metric_Pad1.15x1.40mm_HandSolder; moved to B.Cu
- R10, R18, R19, R8, R9: value 27kΩ -> 4.7kΩ; footprint Resistor_SMD:R_0603_1608Metric -> Resistor_SMD:R_0805_2012Metric_Pad1.15x1.40mm_HandSolder
- R11: value 1kΩ -> 4.7kΩ; footprint Resistor_SMD:R_0603_1608Metric -> Resistor_SMD:R_0805_2012Metric_Pad1.15x1.40mm_HandSolder
- R12: value 4.7MΩ -> 4.7kΩ; footprint Resistor_SMD:R_0603_1608Metric -> Resistor_SMD:R_0805_2012Metric_Pad1.15x1.40mm_HandSolder
- R13: value 470kΩ -> 4.7kΩ; footprint Resistor_SMD:R_0603_1608Metric -> Resistor_SMD:R_0805_2012Metric_Pad1.15x1.40mm_HandSolder
- R14: value 47kΩ -> 4.7kΩ; footprint Resistor_SMD:R_0603_1608Metric -> Resistor_SMD:R_0805_2012Metric_Pad1.15x1.40mm_HandSolder
- R15: footprint Resistor_SMD:R_0603_1608Metric -> Resistor_SMD:R_0805_2012Metric_Pad1.15x1.40mm_HandSolder
- R16, R17: value 510k -> 4.7kΩ; footprint Resistor_SMD:R_0603_1608Metric -> Resistor_SMD:R_0805_2012Metric_Pad1.15x1.40mm_HandSolder
- R2: value 1k -> 4.7kΩ; footprint Resistor_SMD:R_0805_2012Metric -> Resistor_SMD:R_0805_2012Metric_Pad1.15x1.40mm_HandSolder; moved to B.Cu
- R3: value 100 -> 4.7kΩ; footprint Resistor_SMD:R_0805_2012Metric -> Resistor_SMD:R_0805_2012Metric_Pad1.15x1.40mm_HandSolder; moved to B.Cu
- R7: value R_Small -> 4.7kΩ; footprint Resistor_SMD:R_0805_2012Metric -> Resistor_SMD:R_0805_2012Metric_Pad1.15x1.40mm_HandSolder; moved to B.Cu
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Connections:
- D1 pad 1: /Signal conditioning/LEDDrive.IR -> GND
- D1 pad 2: GND -> Net-(D1-Pad2)
- D10 pad 1: /Display/Segment1 -> GND
- D11 pad 1: /Display/Segment2 -> GND
- D12 pad 1: /Display/Segment2 -> GND
- D12 pad 2: Net-(D10-Pad2) -> Net-(D12-Pad2)
- D13 pad 1: /Display/Segment3 -> GND
- D13 pad 2: Net-(D11-Pad2) -> Net-(D13-Pad2)
- D14 pad 1: /Display/Segment3 -> GND
- D14 pad 2: Net-(D10-Pad2) -> Net-(D14-Pad2)
- D15 pad 1: /Display/Segment4 -> GND
- D15 pad 2: Net-(D11-Pad2) -> Net-(D15-Pad2)
- D16 pad 1: /Display/Segment4 -> GND
- D16 pad 2: Net-(D10-Pad2) -> Net-(D16-Pad2)
- D17 pad 1: /Display/Segment5 -> GND
- D17 pad 2: Net-(D11-Pad2) -> Net-(D17-Pad2)
- D18 pad 1: /Display/Segment5 -> GND
- D18 pad 2: Net-(D10-Pad2) -> Net-(D18-Pad2)
- D19 pad 1: /Display/Segment6 -> GND
- D19 pad 2: Net-(D11-Pad2) -> Net-(D19-Pad2)
- D2 pad 1: /Signal conditioning/LEDDrive.IR -> GND
- D2 pad 2: GND -> Net-(D2-Pad2)
- D20 pad 1: /Display/Segment6 -> GND
- D20 pad 2: Net-(D10-Pad2) -> Net-(D20-Pad2)
- D21 pad 1: Net-(D11-Pad2) -> GND
- D21 pad 2: /Display/Segment0 -> Net-(D21-Pad2)
- D22 pad 1: Net-(D10-Pad2) -> GND
- D22 pad 2: /Display/Segment0 -> Net-(D22-Pad2)
- D23 pad 1: Net-(D11-Pad2) -> GND
- D23 pad 2: /Display/Segment1 -> Net-(D23-Pad2)
- D24 pad 1: Net-(D10-Pad2) -> GND
- D24 pad 2: /Display/Segment1 -> Net-(D24-Pad2)
- D25 pad 1: Net-(D11-Pad2) -> GND
- D25 pad 2: /Display/Segment2 -> Net-(D25-Pad2)
- D26 pad 1: Net-(D10-Pad2) -> GND
- D26 pad 2: /Display/Segment2 -> Net-(D26-Pad2)
- D27 pad 1: Net-(D11-Pad2) -> GND
- D27 pad 2: /Display/Segment3 -> Net-(D27-Pad2)
- D28 pad 1: Net-(D11-Pad2) -> GND
- D28 pad 2: /Display/Segment4 -> Net-(D28-Pad2)
- D29 pad 1: Net-(D11-Pad2) -> GND
- D29 pad 2: /Display/Segment5 -> Net-(D29-Pad2)
- D3 pad 1: /Signal conditioning/LEDDrive.Red -> GND
- D3 pad 2: GND -> Net-(D3-Pad2)
- D30 pad 1: Net-(D11-Pad2) -> GND
- D30 pad 2: /Display/Segment6 -> Net-(D30-Pad2)
- D7 pad 1: /Display/Segment0 -> GND
- D7 pad 2: Net-(D11-Pad2) -> Net-(D7-Pad2)
- D8 pad 1: /Display/Segment0 -> GND
- D8 pad 2: Net-(D10-Pad2) -> Net-(D8-Pad2)
- D9 pad 1: /Display/Segment1 -> GND
- D9 pad 2: Net-(D11-Pad2) -> Net-(D9-Pad2)
- J1 pad 1: /5V_power_input -> +5V
- J1 pad 2: /USB interface/Data- -> Net-(J1-Pad2)
- J1 pad 3: /USB interface/Data+ -> Net-(J1-Pad3)
- J2 pad R1: /Signal conditioning/LEDOut.IR -> Net-(J2-PadR1)
- J2 pad S: /Signal conditioning/PhotoDiode -> Net-(J2-PadS)
- J2 pad T: /Signal conditioning/LEDOut.Red -> Net-(J2-PadT)
- JP1 pad 1: /USB interface/Data+ -> +5V
- JP1 pad 2: /Microcontroller/SWIM -> Net-(JP1-Pad2)
- JP2 pad 1: /USB interface/DataTX -> +5V
- JP2 pad 2: /USB interface/Data- -> Net-(JP2-Pad2)
- R1 pad 1: /Signal conditioning/PhotoDiodeInternal -> Net-(JP1-Pad2)
- R1 pad 2: /Microcontroller/ADC_feedback -> Net-(D1-Pad2)
- R10 pad 1: Net-(R10-Pad1) -> Net-(JP11-Pad2)
- R10 pad 2: Net-(R10-Pad2) -> Net-(D10-Pad2)
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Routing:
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- removed copper zone on B.Cu, net /Testing finger board/GND
- removed copper zone on F.Cu, net /Testing finger board/GND
- removed copper zone on B.Cu, net Net-(J3-Pad5)
- removed copper zone on F.Cu, net Net-(J3-Pad5)
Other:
- board size 100 x 100 mm -> 40 x 27 mm
- copper layers 2 -> 4
- board text added: "Display test board Rev B"
- board text removed: "0"
- board text removed: "0.1µA"
- board text removed: "1"
- board text removed: "10"
- board text removed: "100µA"
- board text removed: "10µA"
- board text removed: "1µA"
- board text removed: "2"
- board text removed: "3"
- board text removed: "4"
- board text removed: "5"
- board text removed: "6"
- board text removed: "7"
- board text removed: "8"
- board text removed: "9"
- board text removed: "Current range"
- board text removed: "Development board Rev A"
- board text removed: "Finger simulator Rev A"
- board text removed: "GND"
- board text removed: "Infrared bias"
- board text removed: "Infrared scale"
- board text removed: "MIX"
- board text removed: "Noise scale"
- board text removed: "Programming adapter Rev A"
- board text removed: "Red bias"
- board text removed: "Red scale"
- board text removed: "SWIM"
- board text removed: "Simulated transmissivity"
- board text removed: "UART.TX"
